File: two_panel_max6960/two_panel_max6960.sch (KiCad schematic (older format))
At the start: 11 parts, among them M1 LED-MATRIX-8X8, M2 LED-MATRIX-8X8, P1 CONN_12, P2 CONN_12, P3 CONN_2, U1 MAX6960

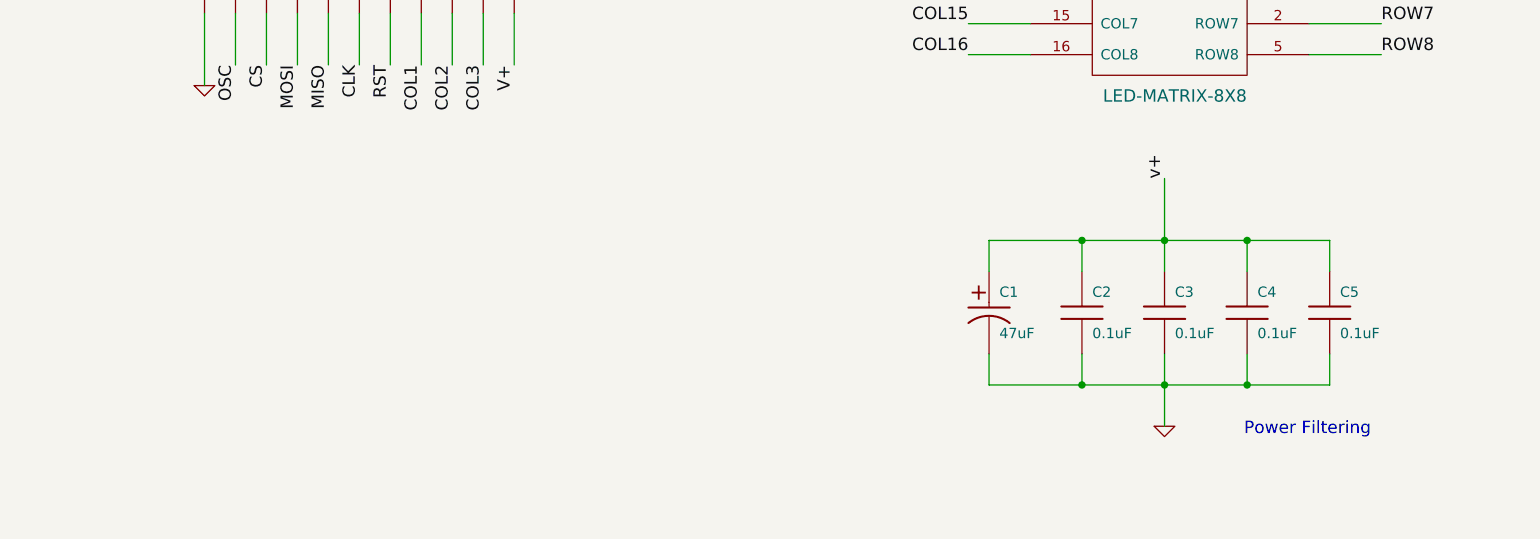
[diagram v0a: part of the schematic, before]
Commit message: Completed initial design of panels (G4) based on the max6960 IC. Created adapter PCB for mounting two 8x8 panels to max6960 controller board. Created version 0.1 of gerber files for both the controller and adapter PCBs.
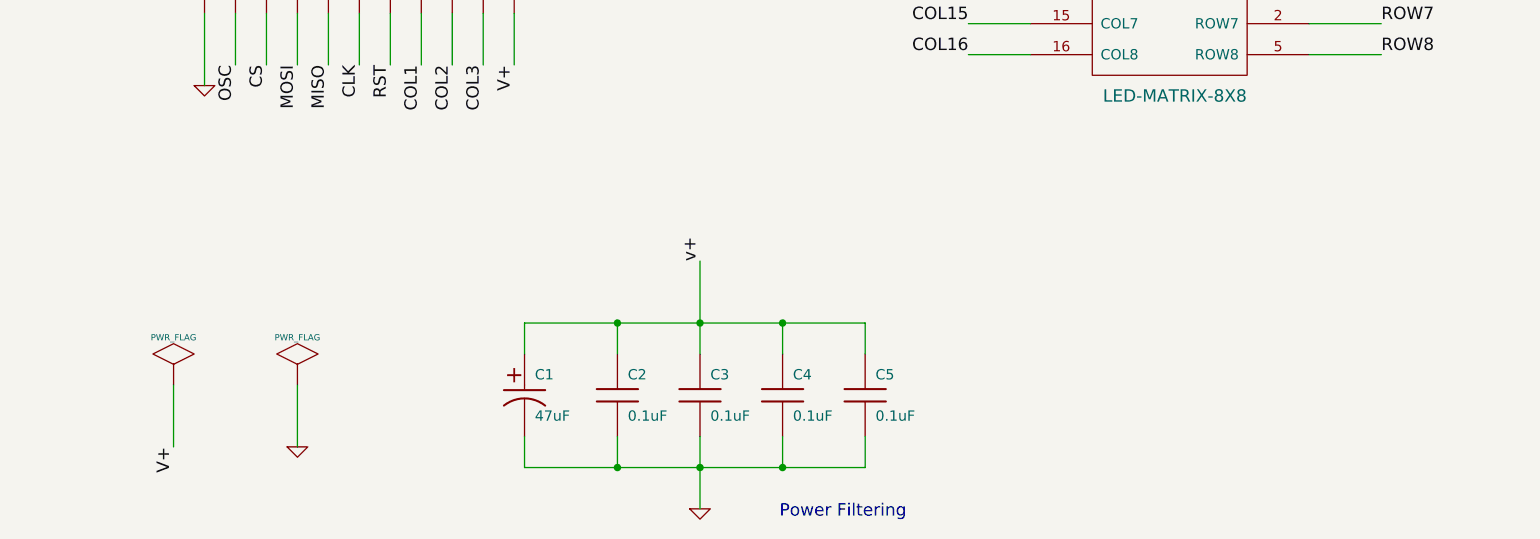
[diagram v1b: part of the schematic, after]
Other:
- moved on the sheet: C1, C2, C3, C4, C5
